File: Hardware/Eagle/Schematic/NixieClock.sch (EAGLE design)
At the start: 16 parts, among them X0 5566-12, X1 5566-12, X2 5566-12, X3 5566-12, X4 5566-12, X5 5566-12

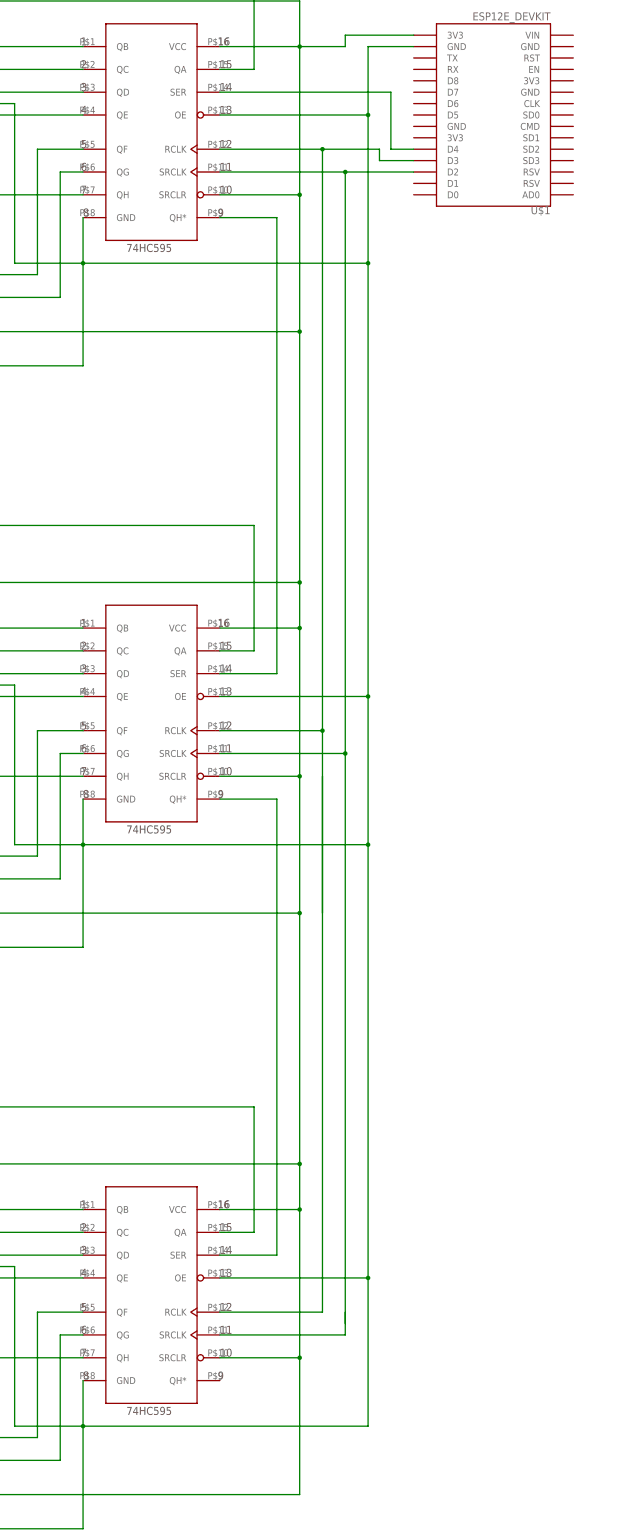
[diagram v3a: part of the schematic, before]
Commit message: Routed further chips' VCC and GND to the node's 3v3 and GND
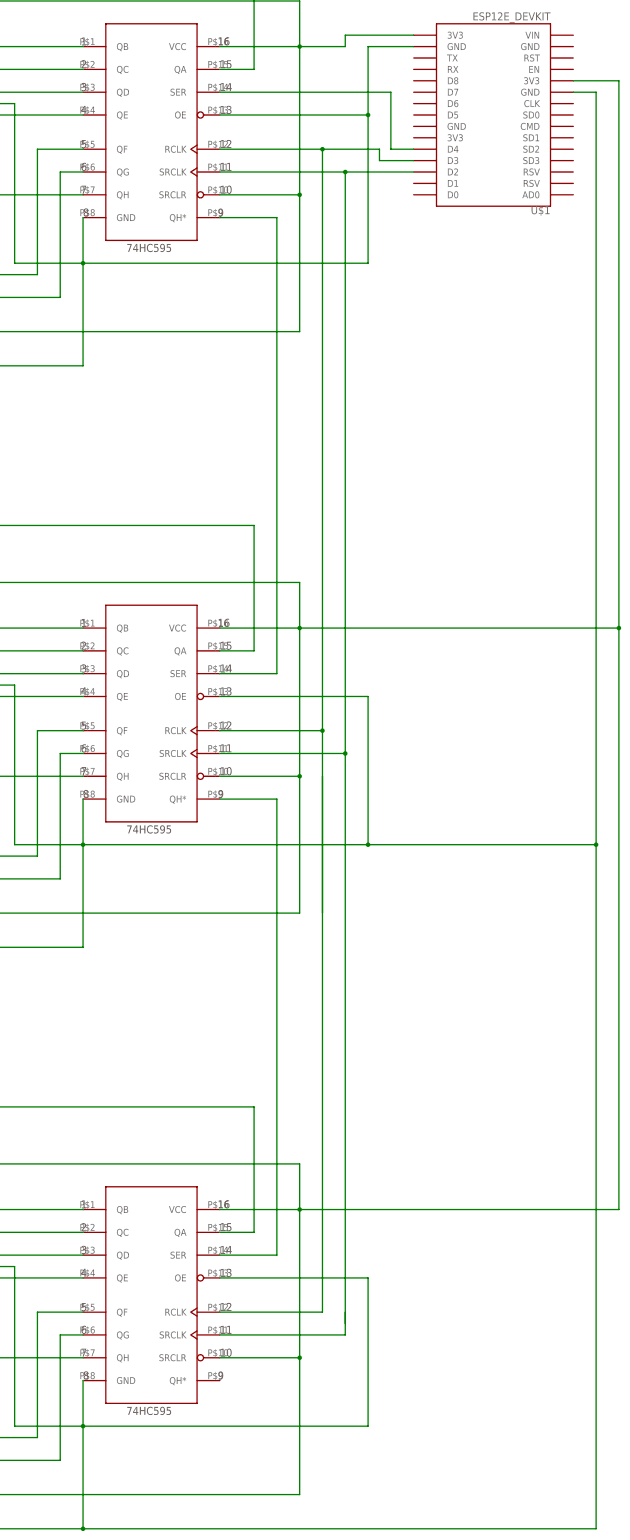
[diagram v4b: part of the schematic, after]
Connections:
- new net N$44: BCD0.VCC, BCD1.VCC, SR0.SRCLR, SR0.VCC, U$1.3V3@2
- new net N$45: BCD0.GND, BCD1.GND, SR0.GND, SR0.OE, U$1.GND@3
- net N$13: now also U$1.3V3@0; no longer BCD0.VCC, BCD1.VCC, SR0.SRCLR, SR0.VCC, U$1.3V3@2
- net N$23: now also U$1.GND@0; no longer BCD0.GND, BCD1.GND, SR0.GND, SR0.OE, U$1.GND@3
